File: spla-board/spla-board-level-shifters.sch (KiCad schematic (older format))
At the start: 22 parts, among them J3 J_BODGE, J6 J_SAMPLE, U15 74LVC8T245, U16 74LVC8T245, U17 74LVC8T245, U20 74LVC8T245, U22 74LVC8T245, U23 74LVC8T245, U24 74LVC8T245, U25 74LVC8T245, U26 74LVC8T245, U27 74LVC8T245, U28 74LVC8T245, U29 74LVC8T245, U30 74LVC8T245, U31 74LVC8T245, U32 74LVC8T245

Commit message: schematic/pcb: Pinswap entire FPGA to put LEDs/TPs on south edge.
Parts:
- J6: footprint Connector_PinHeader_2.54mm:PinHeader_1x04_P2.54mm_Vertical -> Connector_PinHeader_2.54mm:PinHeader_1x06_P2.54mm_Vertical; symbol Connector_Generic:Conn_01x04 -> Connector_Generic:Conn_01x06
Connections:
- net GND: now also J6.1 (Pin_1), J6.6 (Pin_6)
- net TAP_PPU2_HBLANK: now also J6.3 (Pin_3); no longer J6.2 (Pin_2)
- net TAP_PPU2_VBLANK: now also J6.2 (Pin_2); no longer J6.1 (Pin_1)
- net TAP_~BURST~: now also J6.4 (Pin_4); no longer J6.3 (Pin_3)
- net TAP_~CSYNC~: now also J6.5 (Pin_5); no longer J6.4 (Pin_4)
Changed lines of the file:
@@
 FPGA_PPU2_EXTLATCH
 $Comp
-L Connector_Generic:Conn_01x04 J6
+L Connector_Generic:Conn_01x06 J6
 U 1 1 5E9B9595
 P 7250 2700
 F 0 "J6" V 7350 2650 50  0000 L CNN
 F 1 "J_SAMPLE" V 7450 2500 50  0000 L CNN
-F 2 "Connector_PinHeader_2.54mm:PinHeader_1x04_P2.54mm_Vertical" H 7250 2700 50  0001 C CNN
+F 2 "Connector_PinHeader_2.54mm:PinHeader_1x06_P2.54mm_Vertical" H 7250 2700 50  0001 C CNN
 F 3 "~" H 7250 2700 50  0001 C CNN
 F 4 "S1011EC-40-ND" H 7250 2700 50  0001 C CNN "Digikey"
@@
 Wire Wire Line
 	1250 1950 1150 1950
+$Comp
+L power:GND #PWR0235
+U 1 1 5F7459ED
+P 6850 2650
+F 0 "#PWR0235" H 6850 2400 50  0001 C CNN
+F 1 "GND" H 6855 2477 50  0000 C CNN
+F 2 "" H 6850 2650 50  0001 C CNN
+F 3 "" H 6850 2650 50  0001 C CNN
+	1    6850 2650
+	1    0    0    -1
+$EndComp
+$Comp
+L power:GND #PWR0236
+U 1 1 5F75989A
+P 7750 2650
+F 0 "#PWR0236" H 7750 2400 50  0001 C CNN
+F 1 "GND" H 7755 2477 50  0000 C CNN
+F 2 "" H 7750 2650 50  0001 C CNN
+F 3 "" H 7750 2650 50  0001 C CNN
+	1    7750 2650
+	1    0    0    -1
+$EndComp
+Wire Wire Line
+	7750 2500 7550 2500
+Wire Wire Line
+	7750 2500 7750 2650
+Wire Wire Line
+	7050 2500 6850 2500
+Wire Wire Line
+	6850 2500 6850 2650
 $EndSCHEMATC

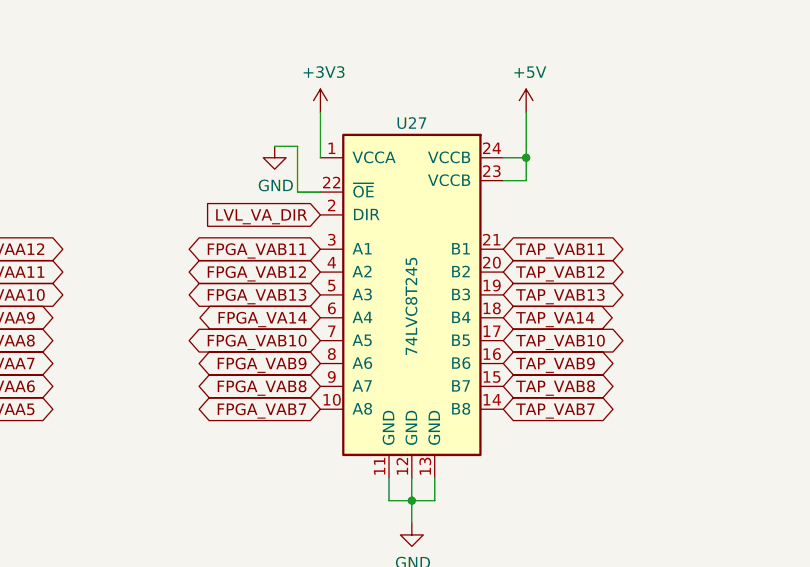
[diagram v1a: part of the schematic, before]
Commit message: pcb/schematic: Rework layout for 0.65mm PPU footprint, as well as other minor issues.
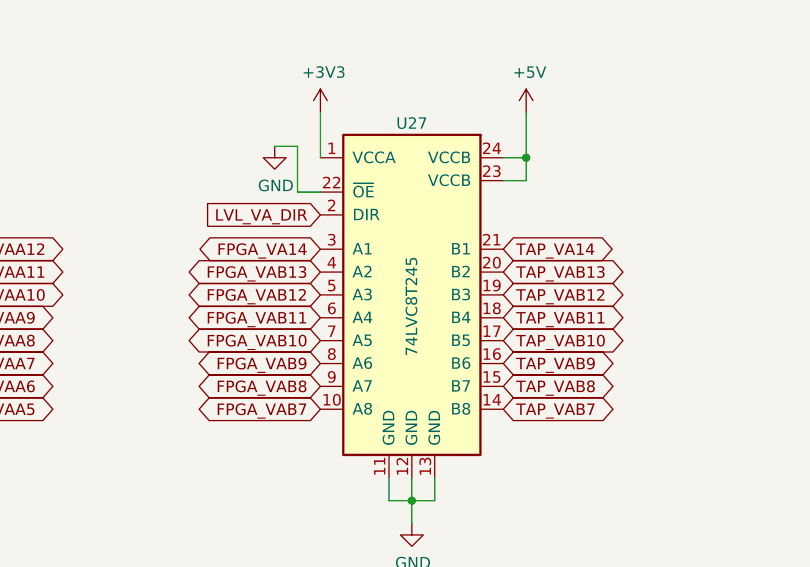
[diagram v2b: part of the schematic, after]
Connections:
- net FPGA_VA14: now also U27.3 (A1); no longer U27.6 (A4)
- net FPGA_VAB11: now also U27.6 (A4); no longer U27.3 (A1)
- net FPGA_VAB12: now also U27.5 (A3); no longer U27.4 (A2)
- net FPGA_VAB13: now also U27.4 (A2); no longer U27.5 (A3)
- net TAP_VA14: now also U27.21 (B1); no longer U27.18 (B4)
- net TAP_VAB11: now also U27.18 (B4); no longer U27.21 (B1)
- net TAP_VAB12: now also U27.19 (B3); no longer U27.20 (B2)
- net TAP_VAB13: now also U27.20 (B2); no longer U27.19 (B3)
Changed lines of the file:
@@
 	1    0    0    -1
 $EndComp
+Text GLabel 9150 9300 2    50   BiDi ~ 0
+TAP_VA14
+Text GLabel 8350 9300 0    50   BiDi ~ 0
+FPGA_VA14
 Text GLabel 9150 9600 2    50   BiDi ~ 0
-TAP_VA14
+TAP_VAB11
+Text GLabel 9150 9500 2    50   BiDi ~ 0
+TAP_VAB12
+Text GLabel 9150 9400 2    50   BiDi ~ 0
+TAP_VAB13
 Text GLabel 8350 9600 0    50   BiDi ~ 0
-FPGA_VA14
-Text GLabel 9150 9300 2    50   BiDi ~ 0
-TAP_VAB11
-Text GLabel 9150 9400 2    50   BiDi ~ 0
-TAP_VAB12
-Text GLabel 9150 9500 2    50   BiDi ~ 0
-TAP_VAB13
-Text GLabel 8350 9300 0    50   BiDi ~ 0
 FPGA_VAB11
+Text GLabel 8350 9500 0    50   BiDi ~ 0
+FPGA_VAB12
 Text GLabel 8350 9400 0    50   BiDi ~ 0
-FPGA_VAB12
-Text GLabel 8350 9500 0    50   BiDi ~ 0
 FPGA_VAB13
 NoConn ~ 11050 1550

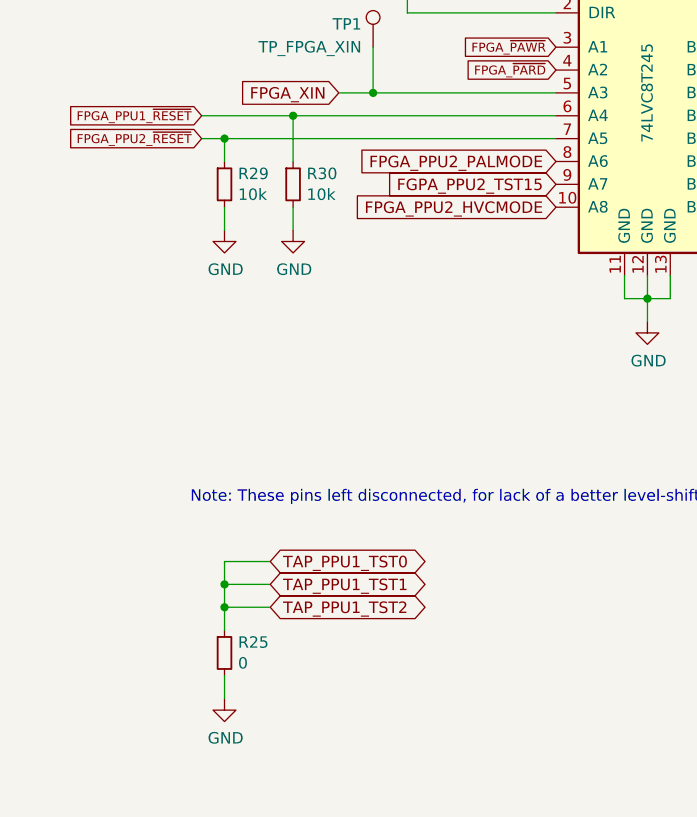
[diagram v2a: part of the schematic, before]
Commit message: schematic/pcb: Remove unnecessary 0-ohm resistors; renumber all parts by value.
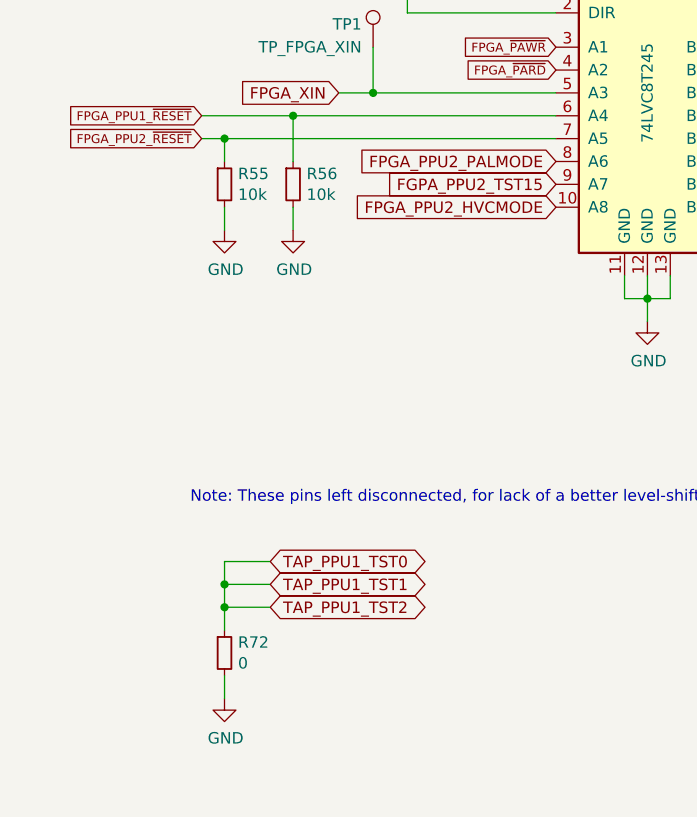
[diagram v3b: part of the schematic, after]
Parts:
- renumbered R29 to R55, R30 to R56, R25 to R72
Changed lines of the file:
@@
 DIR = B-to-A
 $Comp
-L Device:R_Small R25
+L Device:R_Small R72
 U 1 1 5F2D13A9
 P 1250 4200
-F 0 "R25" H 1309 4246 50  0000 L CNN
+F 0 "R72" H 1309 4246 50  0000 L CNN
 F 1 "0" H 1309 4155 50  0000 L CNN
 F 2 "Resistor_SMD:R_0603_1608Metric" H 1250 4200 50  0001 C CNN
@@
 P 1250 2150
 AR Path="/5E50E589/5EB1A3B9" Ref="R?"  Part="1"
-AR Path="/5E50D400/5EB1A3B9" Ref="R29"  Part="1"
-F 0 "R29" H 1309 2196 50  0000 L CNN
+AR Path="/5E50D400/5EB1A3B9" Ref="R55"  Part="1"
+F 0 "R55" H 1309 2196 50  0000 L CNN
 F 1 "10k" H 1309 2105 50  0000 L CNN
 F 2 "Resistor_SMD:R_0603_1608Metric" H 1250 2150 50  0001 C CNN
@@
 P 1550 2150
 AR Path="/5E50E589/5EB52BAA" Ref="R?"  Part="1"
-AR Path="/5E50D400/5EB52BAA" Ref="R30"  Part="1"
-F 0 "R30" H 1609 2196 50  0000 L CNN
+AR Path="/5E50D400/5EB52BAA" Ref="R56"  Part="1"
+F 0 "R56" H 1609 2196 50  0000 L CNN
 F 1 "10k" H 1609 2105 50  0000 L CNN
 F 2 "Resistor_SMD:R_0603_1608Metric" H 1550 2150 50  0001 C CNN

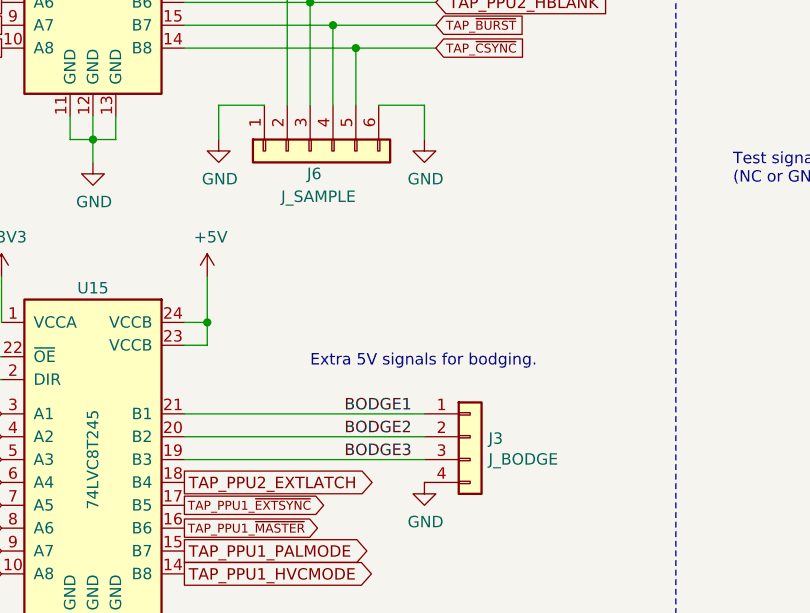
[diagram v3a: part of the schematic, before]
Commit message: schematic/pcb: Renumber connectors (J*).
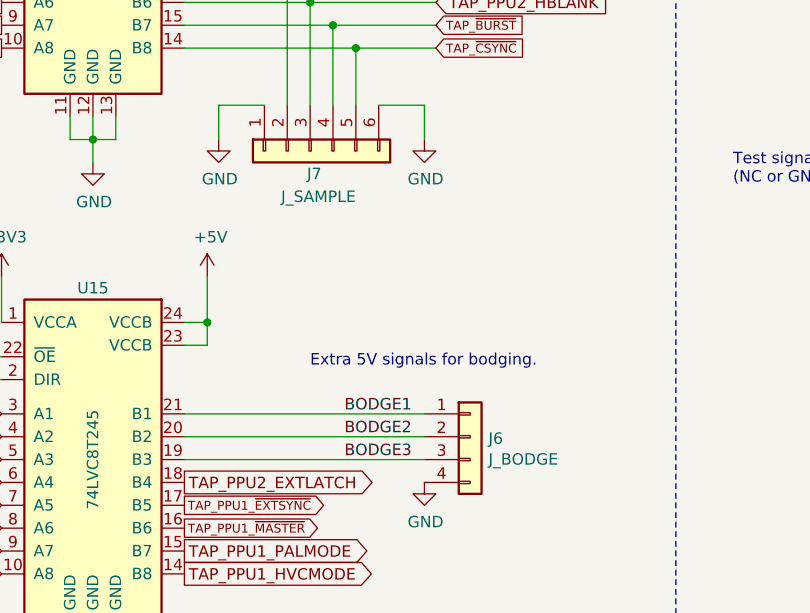
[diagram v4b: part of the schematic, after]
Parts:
- renumbered J3 to J6, J6 to J7
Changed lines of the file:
@@
 	4200 1750 4050 1750
 $Comp
-L Connector_Generic:Conn_01x04 J3
+L Connector_Generic:Conn_01x04 J6
 U 1 1 5E5A824A
 P 7950 3950
-F 0 "J3" H 8030 3942 50  0000 L CNN
+F 0 "J6" H 8030 3942 50  0000 L CNN
 F 1 "J_BODGE" H 8030 3851 50  0000 L CNN
 F 2 "Connector_PinHeader_2.54mm:PinHeader_1x04_P2.54mm_Vertical" H 7950 3950 50  0001 C CNN
@@
 FPGA_PPU2_EXTLATCH
 $Comp
-L Connector_Generic:Conn_01x06 J6
+L Connector_Generic:Conn_01x06 J7
 U 1 1 5E9B9595
 P 7250 2700
-F 0 "J6" V 7350 2650 50  0000 L CNN
+F 0 "J7" V 7350 2650 50  0000 L CNN
 F 1 "J_SAMPLE" V 7450 2500 50  0000 L CNN
 F 2 "Connector_PinHeader_2.54mm:PinHeader_1x06_P2.54mm_Vertical" H 7250 2700 50  0001 C CNN
